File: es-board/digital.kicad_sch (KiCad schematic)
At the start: 17 parts, among them J1 Conn_02x02_Odd_Even, SW1 SW_SPST, U2 ATmega32U4-A, Y1 16MHz Crystal

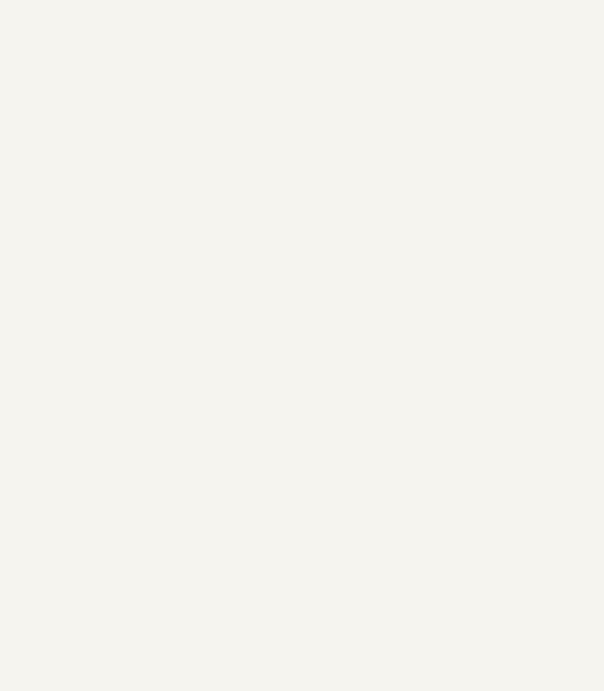
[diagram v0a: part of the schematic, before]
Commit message: Added capacitor circuit
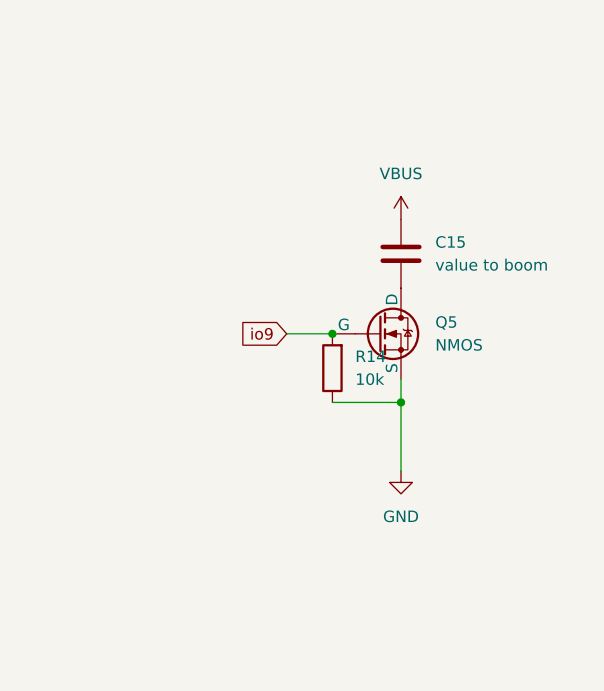
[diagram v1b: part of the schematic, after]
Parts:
- added C15: value to boom, symbol Device:C
- added Q5: NMOS, symbol Simulation_SPICE:NMOS
- added R14: 10k, symbol Device:R
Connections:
- net GND: now also Q5.3 (S), R14.1
- net io9: now also Q5.2 (G), R14.2
- new net: C15.2, Q5.1 (D)
- new net VBUS: C15.1
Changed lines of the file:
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@@
   (junction (at 31.115 69.85) (diameter 0) (color 0 0 0 0)
   )
+  (junction (at 193.04 96.52) (diameter 0) (color 0 0 0 0)
+  )
   (junction (at 61.595 58.42) (diameter 0) (color 0 0 0 0)
   )
@@
   )
   (junction (at 85.725 48.26) (diameter 0) (color 0 0 0 0)
+  )
+  (junction (at 200.66 104.14) (diameter 0) (color 0 0 0 0)
   )
   (junction (at 47.625 69.85) (diameter 0) (color 0 0 0 0)
@@
     (stroke (width 0) (type default))
   )
+  (wire (pts (xy 200.66 111.76) (xy 200.66 104.14))
+    (stroke (width 0) (type default))
+  )
   (wire (pts (xy 88.265 48.26) (xy 85.725 48.26))
     (stroke (width 0) (type default))
@@
   )
   (wire (pts (xy 34.925 146.05) (xy 42.545 146.05))
+    (stroke (width 0) (type default))
+  )
+  (wire (pts (xy 193.04 104.14) (xy 200.66 104.14))
     (stroke (width 0) (type default))
   )
@@
     (stroke (width 0) (type default))
   )
+  (wire (pts (xy 187.96 96.52) (xy 193.04 96.52))
+    (stroke (width 0) (type default))
+  )
   (wire (pts (xy 37.465 90.17) (xy 43.815 90.17))
     (stroke (width 0) (type default))
@@
   )
   (wire (pts (xy 121.285 121.92) (xy 121.285 124.46))
+    (stroke (width 0) (type default))
+  )
+  (wire (pts (xy 200.66 104.14) (xy 200.66 101.6))
     (stroke (width 0) (type default))
   )
@@
     (property "Intersheetrefs" "${INTERSHEET_REFS}" (at 69.7018 60.96 0)
       (effects (font (size 1.27 1.27)) (justify left) hide)
+    )
+  )
+  (global_label "io9" (shape input) (at 187.96 96.52 180) (fields_autoplaced)
+    (effects (font (size 1.27 1.27)) (justify right))
+    (property "Intersheetrefs" "${INTERSHEET_REFS}" (at 182.0115 96.52 0)
+      (effects (font (size 1.27 1.27)) (justify right) hide)
     )
   )
@@
         (path "/e6babbd1-3ad7-4456-9065-760c217e4b6c"
           (reference "C6") (unit 1)
+        )
+      )
+    )
+  )
+  (symbol (lib_id "Device:R") (at 193.04 100.33 180) (unit 1)
+    (in_bom yes) (on_board yes) (dnp no) (fields_autoplaced)
+    (property "Reference" "R14" (at 195.58 99.06 0)
+      (effects (font (size 1.27 1.27)) (justify right))
+    )
+    (property "Value" "10k" (at 195.58 101.6 0)
+      (effects (font (size 1.27 1.27)) (justify right))
+    )
+    (property "Footprint" "" (at 194.818 100.33 90)
+      (effects (font (size 1.27 1.27)) hide)
+    )
+    (property "Datasheet" "~" (at 193.04 100.33 0)
+      (effects (font (size 1.27 1.27)) hide)
+    )
+    (pin "1")
+    (pin "2")
+    (instances
+      (project "es-board"
+        (path "/c2264f68-a6c3-4f6f-b950-c32c683bb958/8eb10449-fef0-4040-85c0-0468d3956b33"
+          (reference "R14") (unit 1)
         )
       )
@@
     )
   )
+  (symbol (lib_id "power:VBUS") (at 200.66 83.82 0) (unit 1)
+    (in_bom yes) (on_board yes) (dnp no) (fields_autoplaced)
+    (property "Reference" "#PWR029" (at 200.66 87.63 0)
+      (effects (font (size 1.27 1.27)) hide)
+    )
+    (property "Value" "VBUS" (at 200.66 78.74 0)
+      (effects (font (size 1.27 1.27)))
+    )
+    (property "Footprint" "" (at 200.66 83.82 0)
+      (effects (font (size 1.27 1.27)) hide)
+    )
+    (property "Datasheet" "" (at 200.66 83.82 0)
+      (effects (font (size 1.27 1.27)) hide)
+    )
+    (pin "1")
+    (instances
+      (project "es-board"
+        (path "/c2264f68-a6c3-4f6f-b950-c32c683bb958/8eb10449-fef0-4040-85c0-0468d3956b33"
+          (reference "#PWR029") (unit 1)
+        )
+      )
+    )
+  )
   (symbol (lib_id "Device:C") (at 34.925 62.23 270) (unit 1)
     (in_bom yes) (on_board yes) (dnp no) (fields_autoplaced)
@@
     )
   )
+  (symbol (lib_id "Device:C") (at 200.66 87.63 0) (unit 1)
+    (in_bom yes) (on_board yes) (dnp no) (fields_autoplaced)
+    (property "Reference" "C15" (at 204.47 86.36 0)
+      (effects (font (size 1.27 1.27)) (justify left))
+    )
+    (property "Value" "value to boom" (at 204.47 88.9 0)
+      (effects (font (size 1.27 1.27)) (justify left))
+    )
+    (property "Footprint" "" (at 201.6252 91.44 0)
+      (effects (font (size 1.27 1.27)) hide)
+    )
+    (property "Datasheet" "~" (at 200.66 87.63 0)
+      (effects (font (size 1.27 1.27)) hide)
+    )
+    (pin "1")
+    (pin "2")
+    (instances
+      (project "es-board"
+        (path "/c2264f68-a6c3-4f6f-b950-c32c683bb958/8eb10449-fef0-4040-85c0-0468d3956b33"
+          (reference "C15") (unit 1)
+        )
+      )
+    )
+  )
   (symbol (lib_id "Device:C") (at 43.815 96.52 0) (unit 1)
     (in_bom yes) (on_board yes) (dnp no) (fields_autoplaced)
@@
     )
   )
+  (symbol (lib_id "Simulation_SPICE:NMOS") (at 198.12 96.52 0) (unit 1)
+    (in_bom yes) (on_board yes) (dnp no) (fields_autoplaced)
+    (property "Reference" "Q5" (at 204.47 95.25 0)
+      (effects (font (size 1.27 1.27)) (justify left))
+    )
+    (property "Value" "NMOS" (at 204.47 97.79 0)
+      (effects (font (size 1.27 1.27)) (justify left))
+    )
+    (property "Footprint" "" (at 203.2 93.98 0)
+      (effects (font (size 1.27 1.27)) hide)
+    )
+    (property "Datasheet" "https://ngspice.sourceforge.io/docs/ngspice-manual.pdf" (at 198.12 109.22 0)
+      (effects (font (size 1.27 1.27)) hide)
+    )
+    (property "Sim.Device" "NMOS" (at 198.12 113.665 0)
+      (effects (font (size 1.27 1.27)) hide)
+    )
+    (property "Sim.Type" "VDMOS" (at 198.12 115.57 0)
+      (effects (font (size 1.27 1.27)) hide)
+    )
+    (property "Sim.Pins" "1=D 2=G 3=S" (at 198.12 111.76 0)
+      (effects (font (size 1.27 1.27)) hide)
+    )
+    (pin "1")
+    (pin "2")
+    (pin "3")
+    (instances
+      (project "es-board"
+        (path "/c2264f68-a6c3-4f6f-b950-c32c683bb958/8eb10449-fef0-4040-85c0-0468d3956b33"
+          (reference "Q5") (unit 1)
+        )
+      )
+    )
+  )
   (symbol (lib_id "Device:R") (at 121.285 118.11 0) (unit 1)
     (in_bom yes) (on_board yes) (dnp no) (fields_autoplaced)
@@
         )
       )
+    )
+  )
+  (symbol (lib_id "power:GND") (at 200.66 111.76 0) (unit 1)
+    (in_bom yes) (on_board yes) (dnp no) (fields_autoplaced)
+    (property "Reference" "#PWR028" (at 200.66 118.11 0)
+      (effects (font (size 1.27 1.27)) hide)
+    )
+    (property "Value" "GND" (at 200.66 116.84 0)
+      (effects (font (size 1.27 1.27)))
+    )
+    (property "Footprint" "" (at 200.66 111.76 0)
+      (effects (font (size 1.27 1.27)) hide)
+    )
+    (property "Datasheet" "" (at 200.66 111.76 0)
+      (effects (font (size 1.27 1.27)) hide)
+    )
+    (pin "1")
+    (instances
+      (project "es-board"
+        (path "/c2264f68-a6c3-4f6f-b950-c32c683bb958/8eb10449-fef0-4040-85c0-0468d3956b33"
+          (reference "#PWR028") (unit 1)
+        )
+      )

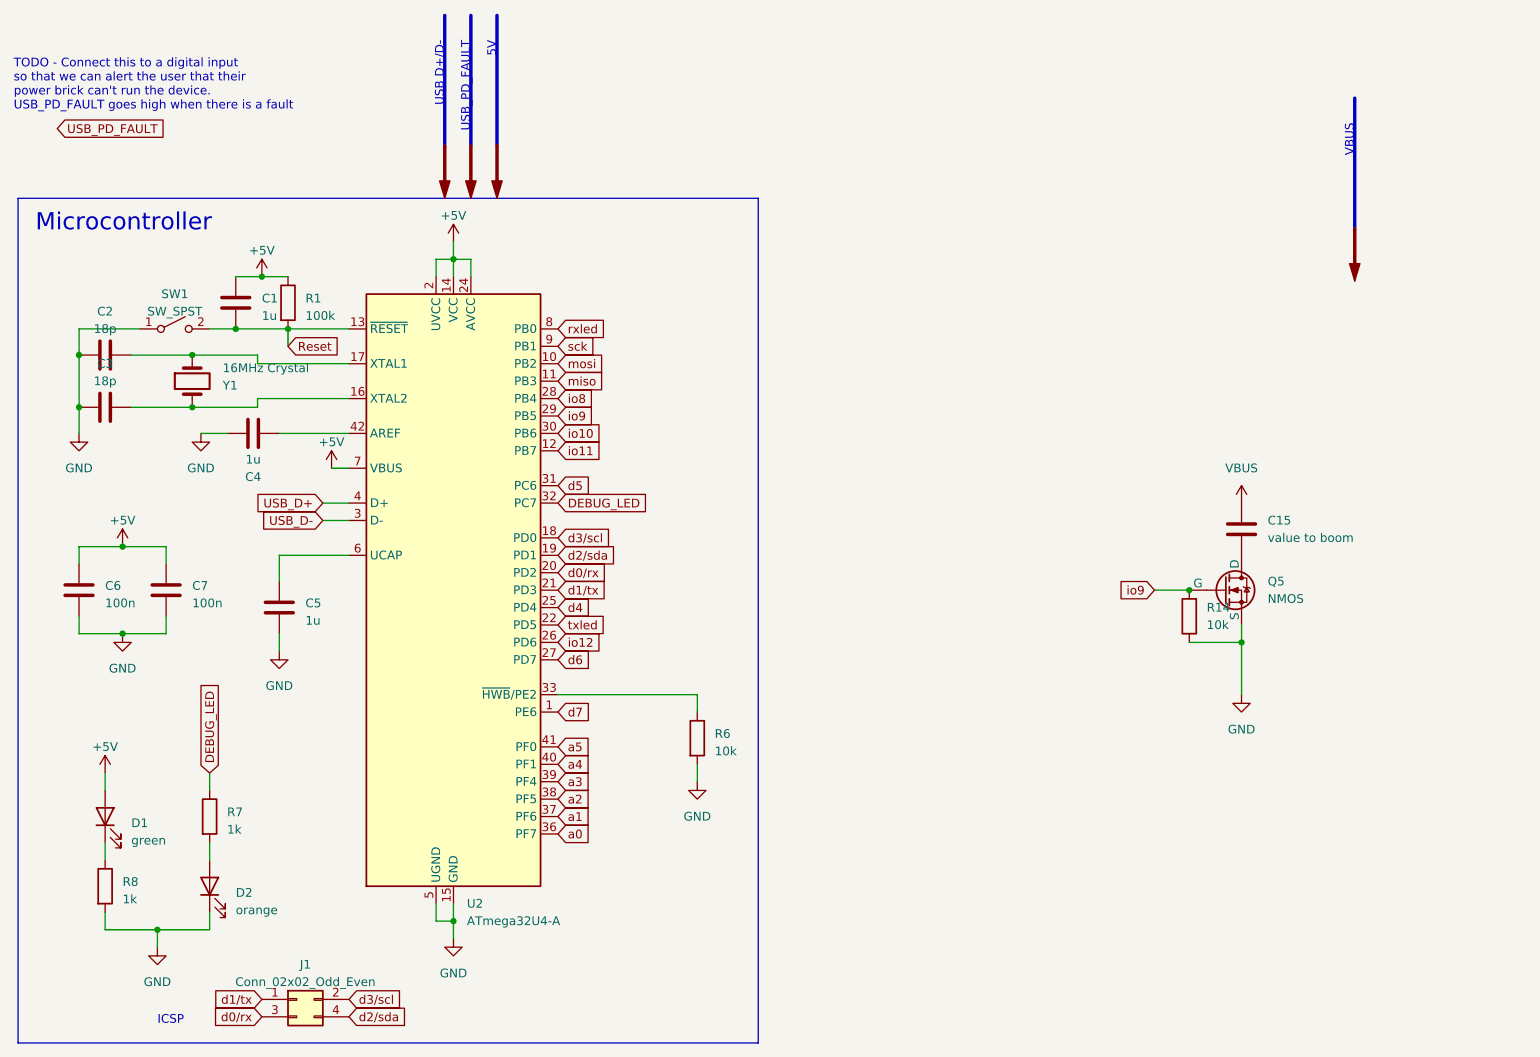
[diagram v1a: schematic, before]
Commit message: Added OLED symbol
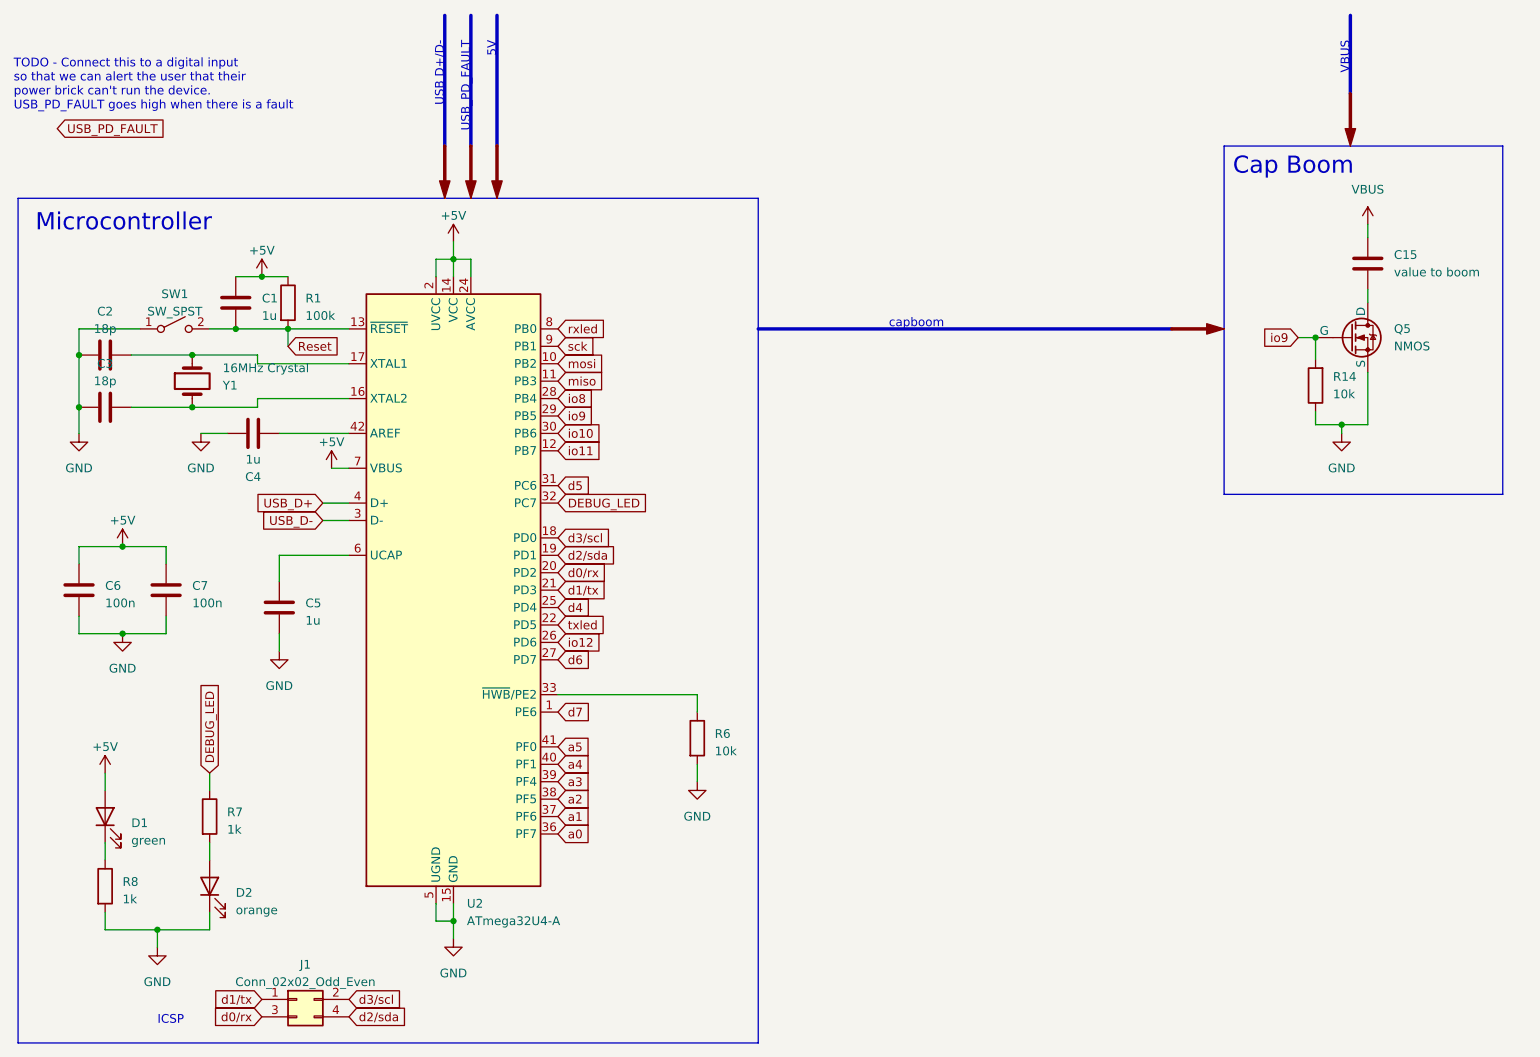
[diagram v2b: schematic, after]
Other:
- note added: "Cap Boom"
- note added: "capboom"
- moved on the sheet: C15, Q5, R14

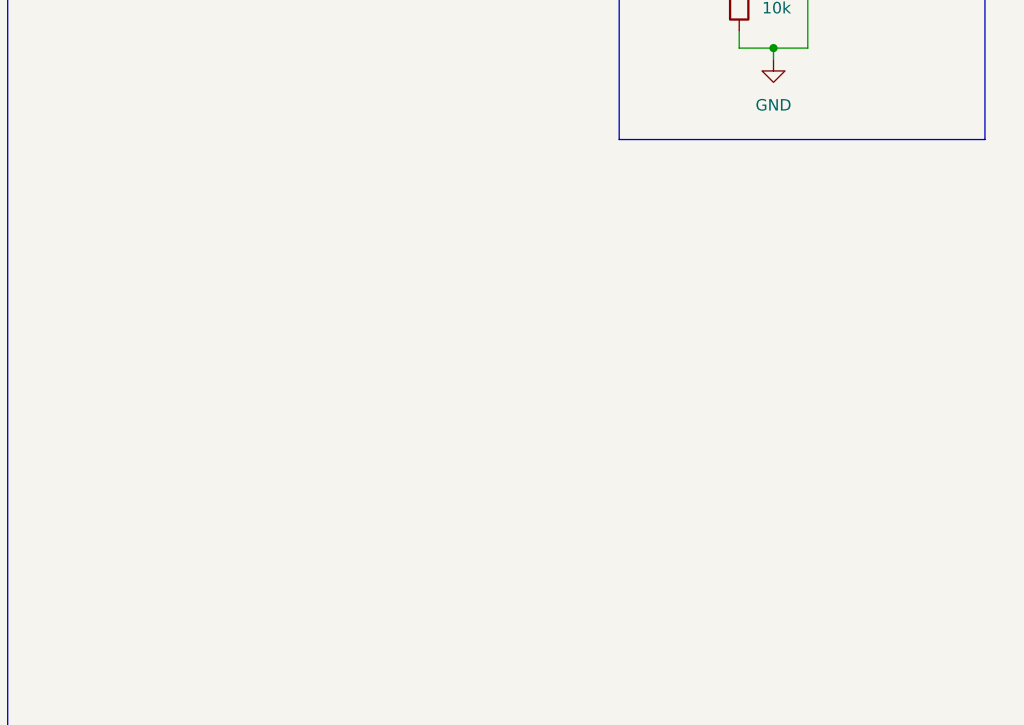
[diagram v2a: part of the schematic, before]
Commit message: Added buttons and OLED
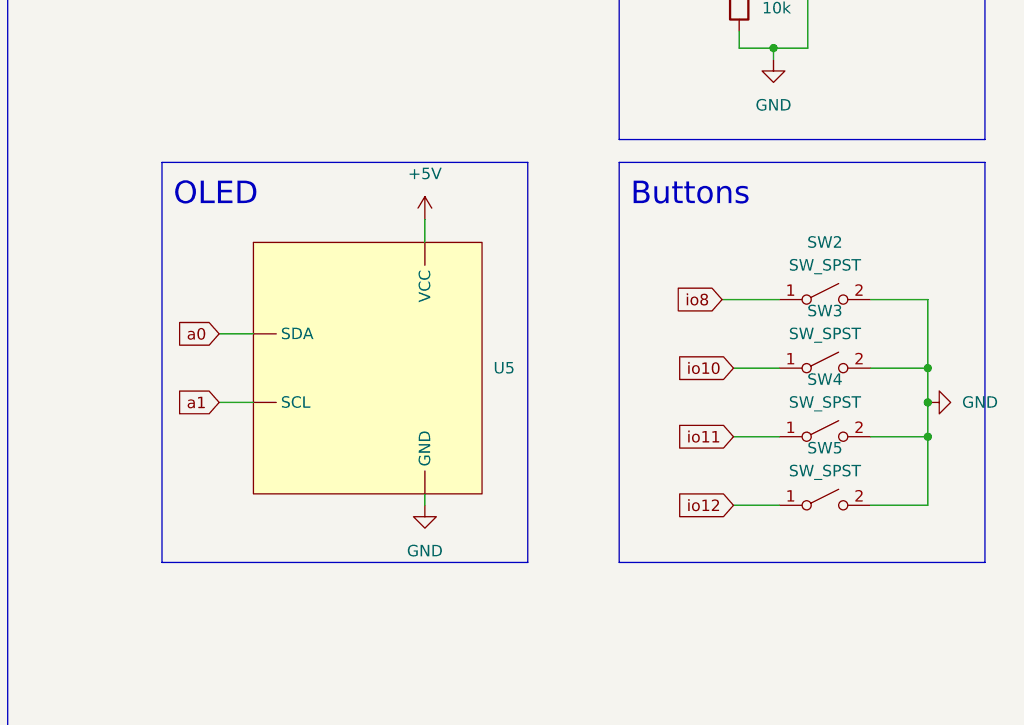
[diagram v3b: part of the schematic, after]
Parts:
- added SW2, SW3, SW4, SW5: SW_SPST, symbol Switch:SW_SPST
- added U5: ~, symbol oled:oled_128x64
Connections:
- net +5V: now also U5. (VCC)
- net GND: now also SW2.2 (B), SW3.2 (B), SW4.2 (B), SW5.2 (B), U5. (VCC)
- net a0: now also U5. (VCC)
- net a1: now also U5. (VCC)
- net io10: now also SW3.1 (A)
- net io11: now also SW4.1 (A)
- net io12: now also SW5.1 (A)
- net io8: now also SW2.1 (A)
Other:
- note added: "Buttons"
- note added: "OLED"

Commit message: Slight cleanups
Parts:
- U5: value ~ -> OLED
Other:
- note added: "SCL,SDA"
- note added: "btn0, btn1, btn2, btn3"
- moved on the sheet: C15, Q5, R14, U5
